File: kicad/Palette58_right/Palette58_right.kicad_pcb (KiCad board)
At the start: 2 copper layers, 145 x 127.8 mm, 124 parts, among them SW1 MSK12C02-HB, SW2 TS-1187A-B-A-B

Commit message: Add mounting holes
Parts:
- added REF**: MountingHole_3.2mm_M3_Pad_Via, MountingHole:MountingHole_3.2mm_M3_Pad_Via, F.Cu at (180.0, -82.0)
- added REF**: MountingHole_3.2mm_M3_Pad_Via, MountingHole:MountingHole_3.2mm_M3_Pad_Via, F.Cu at (166.6, 0.00)
- added REF**: MountingHole_3.2mm_M3_Pad_Via, MountingHole:MountingHole_3.2mm_M3_Pad_Via, F.Cu at (253.5, 7.50)
- added REF**: MountingHole_3.2mm_M3_Pad_Via, MountingHole:MountingHole_3.2mm_M3_Pad_Via, F.Cu at (244.0, -77.5)
- LED1, LED10, LED11, LED12, LED13, LED14, LED15, LED16, LED17, LED18, LED19, LED2, LED20, LED21, LED22, LED23, LED24, LED25, LED26, LED27, LED28, LED29, LED3, LED4, LED5, LED6, LED7, LED8, LED9: value XINGLIGHTXL-1615RGBC-WS2812B -> (none); footprint LED_SMD:XINGLIGHT XL-1615RGBC-WS2812B -> WS2812B
- R1: footprint Resistor_SMD:R_0402_1005Metric -> Resistor
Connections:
- LED1 pad 1: VCC -> (no net)
- LED1 pad 2: Net-(LED1-DOUT) -> GND
- LED1 pad 3: GND -> (no net)
- LED1 pad 4: Net-(LED1-DIN) -> VCC
- LED10 pad 1: VCC -> (no net)
- LED10 pad 2: Net-(LED10-DOUT) -> GND
- LED10 pad 3: GND -> (no net)
- LED10 pad 4: Net-(LED10-DIN) -> VCC
- LED11 pad 1: VCC -> (no net)
- LED11 pad 2: Net-(LED11-DOUT) -> GND
- LED11 pad 3: GND -> (no net)
- LED11 pad 4: Net-(LED11-DIN) -> VCC
- LED12 pad 1: VCC -> (no net)
- LED12 pad 2: Net-(LED12-DOUT) -> GND
- LED12 pad 3: GND -> (no net)
- LED12 pad 4: Net-(LED12-DIN) -> VCC
- LED13 pad 1: VCC -> (no net)
- LED13 pad 2: Net-(LED13-DOUT) -> GND
- LED13 pad 3: GND -> (no net)
- LED13 pad 4: Net-(LED13-DIN) -> VCC
- LED14 pad 1: VCC -> (no net)
- LED14 pad 2: Net-(LED10-DIN) -> GND
- LED14 pad 3: GND -> (no net)
- LED14 pad 4: Net-(LED14-DIN) -> VCC
- LED15 pad 1: VCC -> (no net)
- LED15 pad 2: Net-(LED15-DOUT) -> GND
- LED15 pad 3: GND -> (no net)
- LED15 pad 4: Net-(LED11-DOUT) -> VCC
- LED16 pad 1: VCC -> (no net)
- LED16 pad 2: Net-(LED12-DIN) -> GND
- LED16 pad 3: GND -> (no net)
- LED16 pad 4: Net-(LED16-DIN) -> VCC
- LED17 pad 1: VCC -> (no net)
- LED17 pad 2: Net-(LED17-DOUT) -> GND
- LED17 pad 3: GND -> (no net)
- LED17 pad 4: Net-(LED13-DOUT) -> VCC
- LED18 pad 1: VCC -> (no net)
- LED18 pad 2: Net-(LED14-DIN) -> GND
- LED18 pad 3: GND -> (no net)
- LED18 pad 4: Net-(LED18-DIN) -> VCC
- LED19 pad 1: VCC -> (no net)
- LED19 pad 2: Net-(LED19-DOUT) -> GND
- LED19 pad 3: GND -> (no net)
- LED19 pad 4: Net-(LED15-DOUT) -> VCC
- LED2 pad 1: VCC -> (no net)
- LED2 pad 2: Net-(LED1-DIN) -> GND
- LED2 pad 3: GND -> (no net)
- LED2 pad 4: Net-(LED2-DIN) -> VCC
- LED20 pad 1: VCC -> (no net)
- LED20 pad 2: Net-(LED16-DIN) -> GND
- LED20 pad 3: GND -> (no net)
- LED20 pad 4: Net-(LED20-DIN) -> VCC
- LED21 pad 1: VCC -> (no net)
- LED21 pad 2: Net-(LED21-DOUT) -> GND
- LED21 pad 3: GND -> (no net)
- LED21 pad 4: Net-(LED17-DOUT) -> VCC
- LED22 pad 1: VCC -> (no net)
- LED22 pad 2: Net-(LED18-DIN) -> GND
- LED22 pad 3: GND -> (no net)
- LED22 pad 4: Net-(LED22-DIN) -> VCC
- LED23 pad 1: VCC -> (no net)
- LED23 pad 2: Net-(LED22-DIN) -> GND
- LED23 pad 3: GND -> (no net)
- LED23 pad 4: Net-(LED19-DOUT) -> VCC
- LED24 pad 1: VCC -> (no net)
- LED24 pad 2: Net-(LED20-DIN) -> GND
- LED24 pad 3: GND -> (no net)
- LED24 pad 4: Net-(LED24-DIN) -> VCC
- LED25 pad 1: VCC -> (no net)
- LED25 pad 2: Net-(LED25-DOUT) -> GND
- LED25 pad 3: GND -> (no net)
- LED25 pad 4: Net-(LED21-DOUT) -> VCC
- LED26 pad 1: VCC -> (no net)
- LED26 pad 2: Net-(LED26-DOUT) -> GND
- LED26 pad 3: GND -> (no net)
- LED26 pad 4: Net-(LED25-DOUT) -> VCC
- LED27 pad 1: VCC -> (no net)
- LED27 pad 2: Net-(LED27-DOUT) -> GND
- LED27 pad 3: GND -> (no net)
- LED27 pad 4: Net-(LED26-DOUT) -> VCC
- LED28 pad 1: VCC -> (no net)
- LED28 pad 2: Net-(LED28-DOUT) -> GND
- LED28 pad 3: GND -> (no net)
- LED28 pad 4: Net-(LED27-DOUT) -> VCC
- LED29 pad 1: VCC -> (no net)
- LED29 pad 2: unconnected-(LED29-DOUT-Pad2) -> GND
- LED29 pad 3: GND -> (no net)
- LED29 pad 4: Net-(LED28-DOUT) -> VCC
- LED3 pad 1: VCC -> (no net)
- LED3 pad 2: Net-(LED3-DOUT) -> GND
- LED3 pad 3: GND -> (no net)
- LED3 pad 4: Net-(LED3-DIN) -> VCC
- LED4 pad 1: VCC -> (no net)
- LED4 pad 2: Net-(LED3-DIN) -> GND
- LED4 pad 3: GND -> (no net)
- LED4 pad 4: Net-(LED4-DIN) -> VCC
- LED5 pad 1: VCC -> (no net)
- LED5 pad 2: Net-(LED5-DOUT) -> GND
- LED5 pad 3: GND -> (no net)
- LED5 pad 4: Net-(LED1-DOUT) -> VCC
- LED6 pad 1: VCC -> (no net)
- LED6 pad 2: Net-(LED2-DIN) -> GND
- LED6 pad 3: GND -> (no net)
- LED6 pad 4: Net-(LED10-DOUT) -> VCC
- LED7 pad 1: VCC -> (no net)
- LED7 pad 2: Net-(LED11-DIN) -> GND
- LED7 pad 3: GND -> (no net)
- LED7 pad 4: Net-(LED3-DOUT) -> VCC
- LED8 pad 1: VCC -> (no net)
- LED8 pad 2: Net-(LED4-DIN) -> GND
- LED8 pad 3: GND -> (no net)
- LED8 pad 4: Net-(LED12-DOUT) -> VCC
- LED9 pad 1: VCC -> (no net)
- LED9 pad 2: Net-(LED13-DIN) -> GND
- LED9 pad 3: GND -> (no net)
- LED9 pad 4: Net-(LED5-DOUT) -> VCC
- R1 pad 1: P0.06 -> (no net)
- R1 pad 2: Net-(LED24-DIN) -> (no net)
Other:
- net class Default added: clearance 0.2, trace_width 0.25, via_dia 0.8, via_drill 0.4

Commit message: Add tooling holes
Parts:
- added _92: , ToolingHole, F.Cu at (275.5, -65.5)
- added _93: , ToolingHole, F.Cu at (275.5, 8.50)
- added _94: , ToolingHole, F.Cu at (144.6, 33.6)
- moved C1 1.00 mm to (267.0, -9.25)
- moved C10 1.00 mm to (229.0, -48.2)
- moved C11 1.00 mm to (229.0, -67.2)
- moved C12 1.00 mm to (229.0, -86.2)
- moved C13 1.00 mm to (210.0, -32.8)
- moved C14 1.00 mm to (210.0, -51.8)
- moved C15 1.00 mm to (210.0, -70.8)
- moved C16 1.00 mm to (210.0, -89.8)
- moved C17 1.00 mm to (191.0, -26.8)
- moved C18 1.00 mm to (191.0, -45.8)
- moved C19 1.00 mm to (191.0, -64.8)
- moved C2 1.00 mm to (267.0, -28.2)
- moved C20 1.00 mm to (191.0, -83.8)
- moved C21 1.00 mm to (172.0, -22.8)
- moved C22 1.00 mm to (172.0, -41.8)
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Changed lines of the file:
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@@
     )
   (module Capacitor (layer F.Cu)
-      (at 267 -8.25 0)
+      (at 267 -9.25 0)
     (property "Reference" C1
       (at 0 -0.81)
@@
           )
   (module Capacitor (layer F.Cu)
-      (at 267 -27.25 0)
+      (at 267 -28.25 0)
     (property "Reference" C2
       (at 0 -0.81)
@@
           )
   (module Capacitor (layer F.Cu)
-      (at 267 -46.25 0)
+      (at 267 -47.25 0)
     (property "Reference" C3
       (at 0 -0.81)
@@
           )
   (module Capacitor (layer F.Cu)
-      (at 267 -65.25 0)
+      (at 267 -66.25 0)
     (property "Reference" C4
       (at 0 -0.81)
@@
           )
   (module Capacitor (layer F.Cu)
-      (at 248 -13.25 0)
+      (at 248 -14.25 0)
     (property "Reference" C5
       (at 0 -0.81)
@@
           )
   (module Capacitor (layer F.Cu)
-      (at 248 -32.25 0)
+      (at 248 -33.25 0)
     (property "Reference" C6
       (at 0 -0.81)
@@
           )
   (module Capacitor (layer F.Cu)
-      (at 248 -51.25 0)
+      (at 248 -52.25 0)
     (property "Reference" C7
       (at 0 -0.81)
@@
           )
   (module Capacitor (layer F.Cu)
-      (at 248 -70.25 0)
+      (at 248 -71.25 0)
     (property "Reference" C8
       (at 0 -0.81)
@@
           )
   (module Capacitor (layer F.Cu)
-      (at 229 -28.25 0)
+      (at 229 -29.25 0)
     (property "Reference" C9
       (at 0 -0.81)
@@
           )
   (module Capacitor (layer F.Cu)
-      (at 229 -47.25 0)
+      (at 229 -48.25 0)
     (property "Reference" C10
       (at 0 -0.81)
@@
           )
   (module Capacitor (layer F.Cu)
-      (at 229 -66.25 0)
+      (at 229 -67.25 0)
     (property "Reference" C11
       (at 0 -0.81)
@@
           )
   (module Capacitor (layer F.Cu)
-      (at 229 -85.25 0)
+      (at 229 -86.25 0)
     (property "Reference" C12
       (at 0 -0.81)
@@
           )
   (module Capacitor (layer F.Cu)
-      (at 210 -31.75 0)
+      (at 210 -32.75 0)
     (property "Reference" C13
       (at 0 -0.81)
@@
           )
   (module Capacitor (layer F.Cu)
-      (at 210 -50.75 0)
+      (at 210 -51.75 0)
     (property "Reference" C14
       (at 0 -0.81)
@@
           )
   (module Capacitor (layer F.Cu)
-      (at 210 -69.75 0)
+      (at 210 -70.75 0)
     (property "Reference" C15
       (at 0 -0.81)
@@
           )
   (module Capacitor (layer F.Cu)
-      (at 210 -88.75 0)
+      (at 210 -89.75 0)
     (property "Reference" C16
       (at 0 -0.81)
@@
           )
   (module Capacitor (layer F.Cu)
-      (at 191 -25.75 0)
+      (at 191 -26.75 0)
     (property "Reference" C17
       (at 0 -0.81)
@@
           )
   (module Capacitor (layer F.Cu)
-      (at 191 -44.75 0)
+      (at 191 -45.75 0)
     (property "Reference" C18
       (at 0 -0.81)
@@
           )
   (module Capacitor (layer F.Cu)
-      (at 191 -63.75 0)
+      (at 191 -64.75 0)
     (property "Reference" C19
       (at 0 -0.81)
@@
           )
   (module Capacitor (layer F.Cu)
-      (at 191 -82.75 0)
+      (at 191 -83.75 0)
     (property "Reference" C20
       (at 0 -0.81)
@@
           )
   (module Capacitor (layer F.Cu)
-      (at 172 -21.75 0)
+      (at 172 -22.75 0)
     (property "Reference" C21
       (at 0 -0.81)
@@
           )
   (module Capacitor (layer F.Cu)
-      (at 172 -40.75 0)
+      (at 172 -41.75 0)
     (property "Reference" C22
       (at 0 -0.81)
@@
           )
   (module Capacitor (layer F.Cu)
-      (at 172 -59.75 0)
+      (at 172 -60.75 0)
     (property "Reference" C23
       (at 0 -0.81)
@@
           )
   (module Capacitor (layer F.Cu)
-      (at 172 -78.75 0)
+      (at 172 -79.75 0)
     (property "Reference" C24
       (at 0 -0.81)
@@
           )
   (module Capacitor (layer F.Cu)
-      (at 225.2809651 -7.218606299999999 5)
+      (at 225.1938094 -8.214801 5)
     (property "Reference" C25
       (at 0 -0.81)
@@
           )
   (module Capacitor (layer F.Cu)
-      (at 204.4983717 -4.4551161 10)
+      (at 204.3247236 -5.439923800000001 10)
     (property "Reference" C26
       (at 0 -0.81)
@@
           )
   (module Capacitor (layer F.Cu)
-      (at 184.1283997 0.2047971999999989 15)
+      (at 183.86958059999998 -0.761128600000001 15)
     (property "Reference" C27
       (at 0 -0.81)
@@
           )
   (module Capacitor (layer F.Cu)
-      (at 164.34274359999998 6.7095129999999985 20)
+      (at 164.0007235 5.769820399999999 20)
     (property "Reference" C28
       (at 0 -0.81)
@@
           )
   (module Capacitor (layer F.Cu)
-      (at 145.22265649999997 14.810718199999997 25)
+      (at 144.80003829999995 13.904410399999996 25)
     (property "Reference" C29
       (at 0 -0.81)
@@
 		)
 	)
+  (module ToolingHole (layer F.Cu)
+    (at 275.5 -65.5 0)
+    (property "Reference" _92
+      (at 0 0)
+      (layer F.SilkS)
+      hide
+      (effects
+        (font
+          (size 1 1)
+          (thickness 0.15)
+        )
+      )
+    )
+		(property "Value" ""
+			(at 0 0)
+			(layer "F.Fab")
+      hide
+			(effects
+				(font
+					(size 1 1)
+					(thickness 0.15)
+				)
+			)
+		)
+    (pad "1" thru_hole circle
+      (at 0 0)
+      (size 1.152 1.152)
+      (drill 1.152)
+      (layers *.Cu *.SilkS *.Mask)
+			(remove_unused_layers no)
+			(zone_connect 2)
+    )
+  )
+  (module ToolingHole (layer F.Cu)
+    (at 275.5 8.5 0)
+    (property "Reference" _93
+      (at 0 0)
+      (layer F.SilkS)
+      hide
+      (effects
+        (font
+          (size 1 1)
+          (thickness 0.15)
+        )
+      )
+    )
+		(property "Value" ""
+			(at 0 0)
+			(layer "F.Fab")
+      hide
+			(effects
+				(font
+					(size 1 1)
+					(thickness 0.15)
+				)
+			)
+		)
+    (pad "1" thru_hole circle
+      (at 0 0)
+      (size 1.152 1.152)
+      (drill 1.152)
+      (layers *.Cu *.SilkS *.Mask)
+			(remove_unused_layers no)
+			(zone_connect 2)
+    )
+  )
+  (module ToolingHole (layer F.Cu)
+    (at 144.59789619999998 33.5836288 25)
+    (property "Reference" _94
+      (at 0 0)
+      (layer F.SilkS)
+      hide
+      (effects
+        (font
+          (size 1 1)
+          (thickness 0.15)
+        )
+      )
+    )
+		(property "Value" ""
+			(at 0 0)
+			(layer "F.Fab")
+      hide
+			(effects
+				(font
+					(size 1 1)
+					(thickness 0.15)
+				)
+			)
+		)
+    (pad "1" thru_hole circle
+      (at 0 0)
+      (size 1.152 1.152)
+      (drill 1.152)
+      (layers *.Cu *.SilkS *.Mask)
+			(remove_unused_layers no)
+			(zone_connect 2)
+    )
+  )
   (gr_line (start 133.5 -77) (end 133.5 13.49672123132001) (angle 90) (layer Edge.Cuts) (width 0.15))
 (gr_line (start 133.88704391488255 15.425616266911675) (end 141.1025645090292 32.68154764670044) (angle 90) (layer Edge.Cuts) (width 0.15))

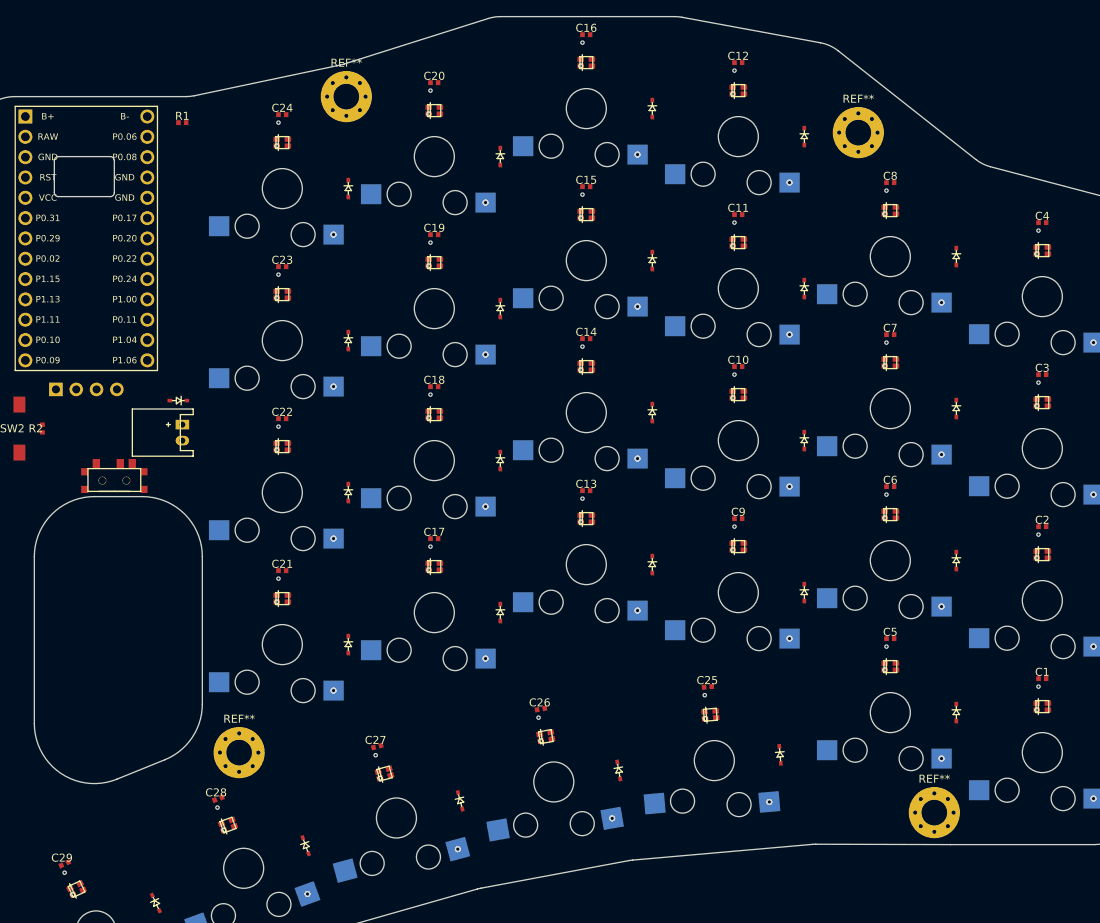
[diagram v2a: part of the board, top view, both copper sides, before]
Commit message: fix: fix capacitor and via placement
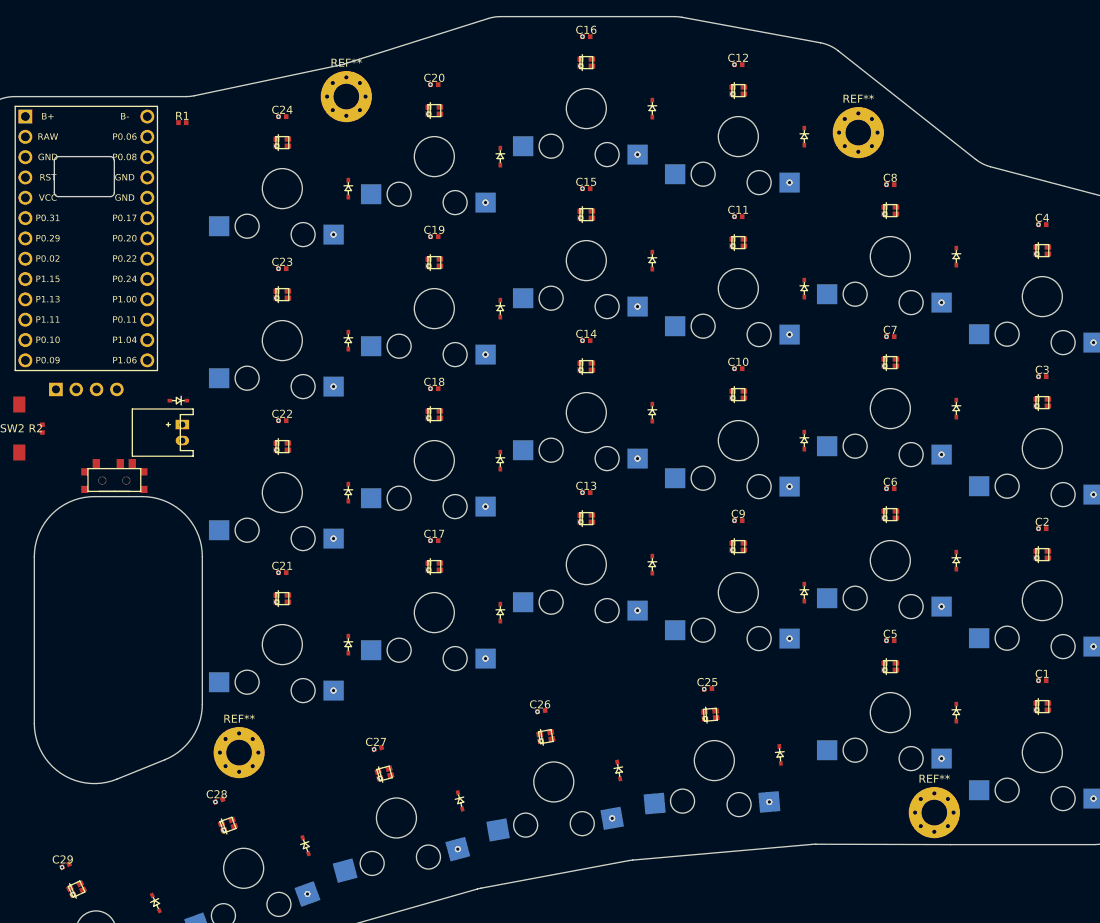
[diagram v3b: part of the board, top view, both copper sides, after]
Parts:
- moved C27 0.25 mm to (183.9, -0.52)
- moved C25 0.25 mm to (225.2, -7.97)
- moved C1 0.25 mm to (267.0, -9.00)
- moved C10 0.25 mm to (229.0, -48.0)
- moved C11 0.25 mm to (229.0, -67.0)
- moved C12 0.25 mm to (229.0, -86.0)
- moved C13 0.25 mm to (210.0, -32.5)
- moved C14 0.25 mm to (210.0, -51.5)
- moved C15 0.25 mm to (210.0, -70.5)
- moved C16 0.25 mm to (210.0, -89.5)
- moved C17 0.25 mm to (191.0, -26.5)
- moved C18 0.25 mm to (191.0, -45.5)
- moved C19 0.25 mm to (191.0, -64.5)
- moved C2 0.25 mm to (267.0, -28.0)
- moved C20 0.25 mm to (191.0, -83.5)
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
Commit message: Update right half
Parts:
- removed C1, C10, C11, C12, C13, C14, C15, C16, C17, C18, C19, C2, C20, C21, C22, C23, C24, C25, C26, C27, C28, C29, C3, C4, C5, C6, C7, C8, C9: 100nF, Capacitor
- removed D30: 1N5819, ComboDiode
- removed LED1, LED10, LED11, LED12, LED13, LED14, LED15, LED16, LED17, LED18, LED19, LED2, LED20, LED21, LED22, LED23, LED24, LED25, LED26, LED27, LED28, LED29, LED3, LED4, LED5, LED6, LED7, LED8, LED9: , WS2812B
- removed R1: 330Ω, Resistor
- removed R2: 10kΩ, Resistor
- removed the REF** at (180.0, -82.0)
- removed the REF** at (244.0, -77.5)
- removed _92, _93, _94: , ToolingHole
- added REF**: MountingHole_3.2mm_M3_Pad_Via, MountingHole:MountingHole_3.2mm_M3_Pad_Via, F.Cu at (244.0, -76.5)
- added REF**: MountingHole_3.2mm_M3_Pad_Via, MountingHole:MountingHole_3.2mm_M3_Pad_Via, F.Cu at (180.0, -81.5)
- added _34: , ToolingHole, F.Cu at (275.5, -65.5)
- added _35: , ToolingHole, F.Cu at (275.5, 8.50)
- added _36: , ToolingHole, F.Cu at (144.6, 33.6)
- moved OLED1 12.4 mm to (141.5, -44.0), turned to 90 degrees
- moved SW2 1.41 mm to (138.0, -39.5)
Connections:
- MCU1 pad 19: row_1 -> SDA
- MCU1 pad 20: row_2 -> SCL
- MCU1 pad 21: row_3 -> row_1
- MCU1 pad 22: row_4 -> row_2
- MCU1 pad 23: row_5 -> row_3
- MCU1 pad 24: P0.11 -> row_4
- MCU1 pad 25: SCL -> row_5
- MCU1 pad 26: SDA -> P1.06
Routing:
- net col_1: track 0.00 -> 206.1 mm, vias 0 -> 1
- net col_2: track 0.00 -> 190.7 mm, vias 0 -> 3
- net col_3: track 0.00 -> 175.7 mm, vias 0 -> 3
- net row_4: track 0.00 -> 164.3 mm
- net col_4: track 0.00 -> 164.0 mm, vias 0 -> 3
- net row_5: track 0.00 -> 162.4 mm
- net row_1: track 0.00 -> 149.9 mm
- net row_3: track 0.00 -> 147.1 mm
- net col_5: track 0.00 -> 146.6 mm, vias 0 -> 2
- net row_2: track 0.00 -> 140.2 mm
- net col_6: track 0.00 -> 131.5 mm
- net B+: track 0.00 -> 62.1 mm
- net RST: track 0.00 -> 37.8 mm
- net VCC: track 0.00 -> 35.2 mm
- net SDA: track 0.00 -> 25.9 mm
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- added copper zone on B.Cu, net GND
- added copper zone on F.Cu, net GND
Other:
- outline, holes or cut-outs redrawn
- net class Default removed
